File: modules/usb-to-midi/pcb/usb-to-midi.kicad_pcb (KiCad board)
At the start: 2 copper layers, 17.5 x 107.3 mm, 22 parts, among them J1 USB Type B Vertical, J2 Thonkiconn ST, J3 JST XH 1x2, U1 ATmega8U2-AU, Y1 16mhz

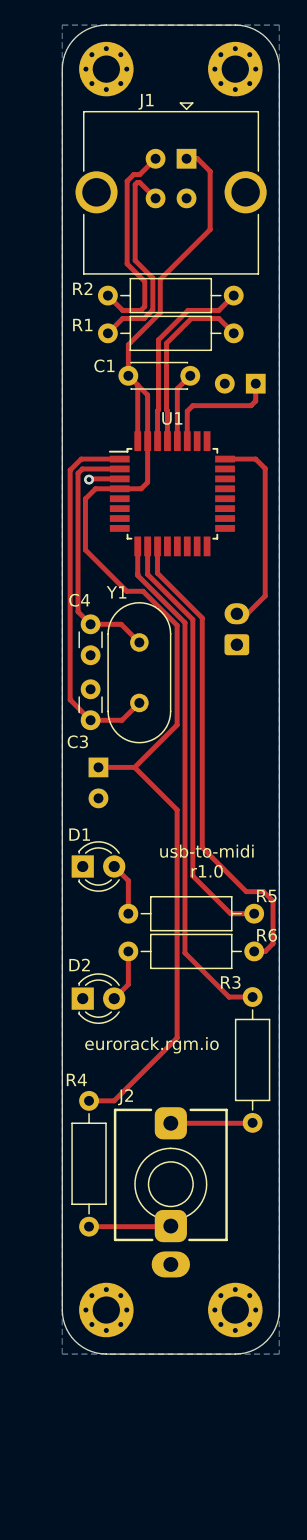
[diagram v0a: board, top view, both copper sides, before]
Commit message: modules: usb-to-midi: revision A (redesign)
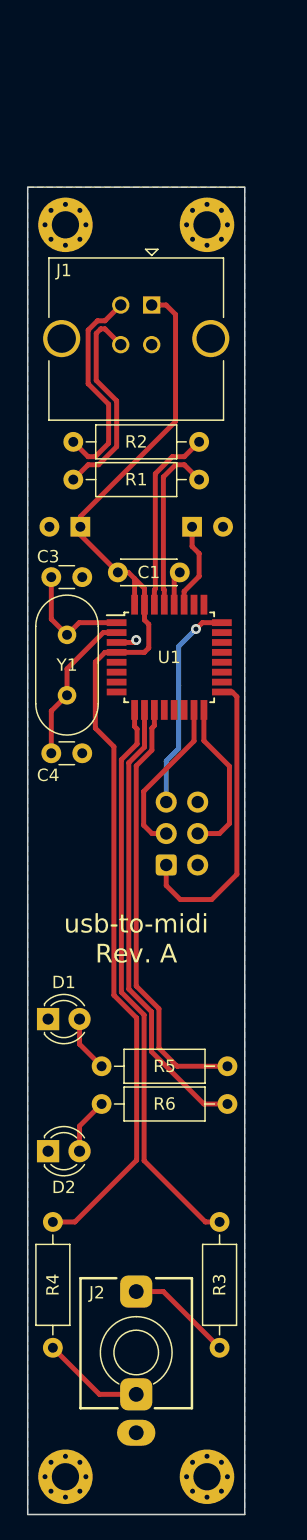
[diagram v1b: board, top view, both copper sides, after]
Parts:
- added REF**: Eurorack_PCB_4HP, eurorack:Eurorack_PCB_4HP, F.Cu at (149.7, 106.8)
- added REF**: OSHW-Symbol_6.7x6mm_SilkScreen, Symbol:OSHW-Symbol_6.7x6mm_SilkScreen, B.Cu at (149.7, 135.9)
- J1: footprint eurorack:USB_B_Vertical -> Connector_USB:USB_B_TE_5787834_Vertical
- J3: value JST XH 1x2 -> ISP; footprint Connector_JST:JST_XH_B2B-XH-A_1x02_P2.50mm_Vertical -> Connector_IDC:IDC-Header_2x03_P2.54mm_Vertical
- Y1: value 16mhz -> 16MHz
- moved C2 19.5 mm to (145.2, 80.6), turned to 180 degrees
- moved J3 18.7 mm to (152.2, 108.0), turned to 0 degrees
- moved R3 18.4 mm to (156.5, 146.9)
- moved C1 16.4 mm to (153.2, 84.3), turned to 180 degrees
- moved J2 13.9 mm to (149.7, 147.3)
- moved H3 13.9 mm to (144.0, 157.4)
- moved H4 13.7 mm to (155.4, 157.4)
- moved U1 13.2 mm to (152.4, 91.2)
- moved H1 13.0 mm to (144.0, 56.3)
- moved H2 12.8 mm to (155.4, 56.3)
- moved C5 12.6 mm to (154.2, 80.6), turned to 0 degrees
- moved D1 12.6 mm to (142.6, 120.4)
- moved D2 12.6 mm to (142.6, 131.1)
- moved R5 12.5 mm to (157.1, 124.2)
- moved R6 12.5 mm to (157.1, 127.3)
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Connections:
- C1 pad 1: +5V -> GND
- C1 pad 2: GND -> +5V
- H1 pad 1: (no net) -> GND
- H2 pad 1: (no net) -> GND
- H3 pad 1: (no net) -> GND
- H4 pad 1: (no net) -> GND
- J3 pad 1: GND -> MISO
- J3 pad 2: dw -> unconnected-(J3-Pad2)
- U1 pad 10: LED1 -> LED2
- U1 pad 11: LED2 -> LED1
- U1 pad 15: unconnected-(U1-Pad15) -> SCK
- U1 pad 16: unconnected-(U1-Pad16) -> MOSI
- U1 pad 17: unconnected-(U1-Pad17) -> MISO
- U1 pad 24: dw -> RESET
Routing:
- net MISO: track 0.00 -> 24.4 mm
- net Net-(C3-Pad1): track 29.3 -> 9.60 mm
- net RESET: track 0.00 -> 17.3 mm, vias 0 -> 1
- net dw: track 16.0 -> 0.00 mm
- net SCK: track 0.00 -> 13.1 mm
- net MOSI: track 0.00 -> 12.9 mm
- net +5V: track 102.7 -> 92.5 mm
- net Net-(C4-Pad1): track 20.2 -> 12.6 mm
- net UART_TX: track 40.8 -> 45.9 mm
- net GND: track 7.21 -> 4.46 mm
- net Net-(C5-Pad1): track 9.18 -> 7.03 mm
- net Net-(J2-PadT): track 6.62 -> 8.61 mm
- net Net-(J2-PadR): track 6.62 -> 8.29 mm
- net LED2: track 38.0 -> 36.8 mm
- net LED1: track 33.8 -> 34.8 mm
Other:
- board size 17.5 x 107.3 mm -> 17.5 x 107.2 mm
- board text added: "usb-to-midi Rev. A"
- board text removed: "usb-to-midi r1.0"
